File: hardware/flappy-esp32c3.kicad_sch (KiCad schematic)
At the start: 57 parts, among them J1 USB-C-Breakout 16P, J2 LiPo 1S 500 mAh, J3 OLED SSD1306 SPI, J4 Arcade-Taster, SW1 Ein/Aus, U1 ESP32-C3-WROOM-02-N4, U2 MCP73831-2-OT, U3 AP2112K-3.3

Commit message: Layout an den Schaltplan angleichen und auf 72 x 51 mm verkleinern
Abgleich Schaltplan <-> Layout
-----------------------------
Der Schaltplan war von Hand nachbearbeitet worden: R17/R18 (5k1) als
CC-Widerstaende an J1-5/J1-6. Weder gen/design.py noch die Platinendatei
kannten sie - die Platine haette keine CC-Widerstaende gehabt und mit einer
C-nach-C-Leitung kein VBUS bekommen.

R17/R18 stehen jetzt mit den Netzen CC1/CC2 in gen/design.py, J1-5 und J1-6
sind aus NO_CONNECT heraus. Sonst waren beide Dateien deckungsgleich.
Nach der Neuerzeugung: 0 Abweichungen (unabhaengig nachgerechnet).

Flaeche und Handbestueckbarkeit
-------------------------------
90 x 60 mm (5400 mm2) -> 72 x 51 mm (3672 mm2), 32 Prozent weniger.

Die alte Platine war zu 27 Prozent gefuellt und hatte trotzdem Stellen mit
0,15 mm Umrissabstand (LS1/R13, C9/R5, C9/U1, C8/R6) - der Platz lag als
leeres Band herum statt zwischen den Bauteilen. Jetzt gilt als pruefbare
Regel LOETABSTAND = 0,8 mm und RANDABSTAND = 0,5 mm; kleinster Wert im
Entwurf 0,82 mm. chk_place.py bricht ab, wenn es enger wird.

Leiterbahnen 843 -> 725 mm, Vias 113 -> 87, laengstes Rueckseitenstueck
10,8 -> 5,4 mm. C8 am Modulpin 10,8 -> 5,0 mm.

Weitere Befunde
---------------
* Die VBAT-Kuehlflaeche des Ladereglers lag nicht am Gehaeuse von U2,
  sondern nur ueber eine 0,5-mm-Bahn angebunden daneben - thermisch
  wirkungslos. Sie liegt jetzt unmittelbar am VBAT-Pad (122 mm2).
  chk_place.py prueft neu, dass jede NETZONE ein Pad ihres Netzes enthaelt;
  sonst wirft KiCad sie beim Fuellen als Insel wieder weg.
* Der Verdrahter reservierte nur fuer die eingeklemmten Masse-Mittelpins
  vorab ein Via. D1-5 (VBUS am ESD-Array) ist genauso eingeklemmt und fehlte.
  Liste heisst jetzt VORAB_VIA und nimmt den Netznamen aus der Netzliste.
* Die bauteil- und bahnfreien Flaechen unter Funkmodul und USB-C-Breakout
  waren als feste Koordinaten im Verdrahter verdrahtet. Sie werden jetzt aus
  der Platzierung abgeleitet und wandern beim Ve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
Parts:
- R17, R18: value 5.1k -> 5k1
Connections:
- net CC1: now reaches J1.5 (Pin_5), R17.1
- net CC2: now reaches J1.6 (Pin_6), R18.1
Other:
- note added: "Nur bestuecken, wenn das Breakout selbst keine CC-Widerstaende traegt."
- note added: "R17/R18 = 5k1 (Rd): ohne sie liefert eine C-nach-C-Leitung kein VBUS."

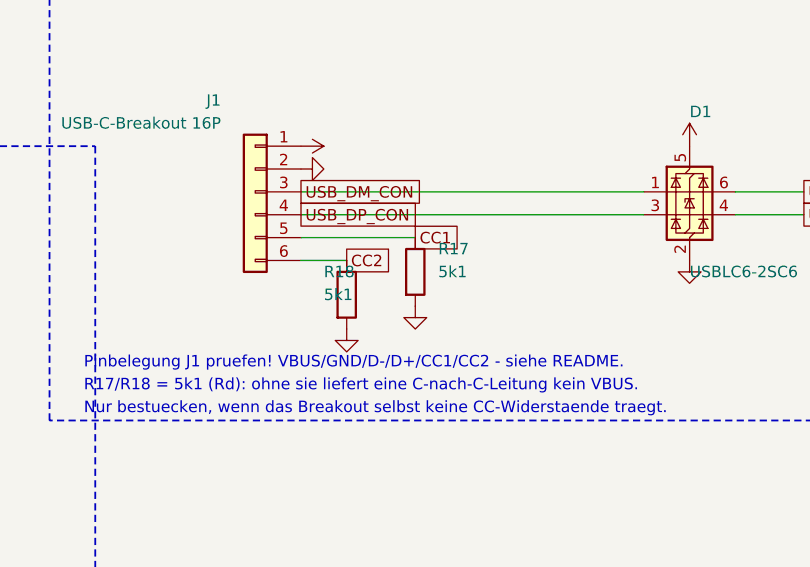
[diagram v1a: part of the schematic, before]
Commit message: Pruefbericht nachgerechnet: Wert nach .sch, Pfade portabel, Repo aufgeraeumt
Nachgeprueft wurden die Befunde F1-F5 eines externen Berichts. F1, F2 und F3
sind berechtigt, F4 und F5 sind bereits dokumentierte Handlungspunkte, keine
Fehler. Die Messwerte des Berichts gehoeren zu Revision A (90 x 60 mm,
371 Bahnen) und stimmen bis auf zwei Abstaende, die von der Masseseite der
Kondensatoren gemessen wurden.

.sch als Master
---------------
Vollstaendiger Abgleich des erzeugten Schaltplans gegen die von Hand
gezeichnete Fassung auf main: 57 Bauteile, 41 Netze, gleiche Footprints,
gleiche Nichtanschluesse - genau eine Abweichung. R17/R18 hiessen von Hand
5.1k, in design.py 5k1. Der Schaltplan gewinnt: design.py sagt jetzt 5.1k.

Der Wertepruefer in tests.py kannte die Schreibweise mit Dezimalpunkt nicht
und haette 5.1k als unlesbar gemeldet. Er nimmt jetzt beide Formen (6k8 und
5.1k); _wert() rechnete schon vorher beide richtig um.

F2: feste macOS-Pfade
---------------------
erzeugen.sh, gen/design.py und gen/tests_stufe3.py hatten
/Applications/KiCad/... fest verdrahtet und brachen auf Linux und Windows ab.
Alle drei suchen jetzt selbst: eigene Umgebungsvariable, dann PATH bzw.
KICAD*_SYMBOL_DIR/KICAD*_FOOTPRINT_DIR, dann die ueblichen Installationsorte
von macOS, Linux und Windows. Notausgang sind FLAPPY_KICAD_CLI,
FLAPPY_KICAD_SYMBOLS und FLAPPY_KICAD_FOOTPRINTS. Findet erzeugen.sh kein
kicad-cli, bricht es gleich am Anfang ab statt auf halbem Weg.

F3: Git-Hygiene
---------------
.DS_Store (zwei Stueck) und _restore_backup_2026-08-25T08-33-44-858/ waren
getrackt, obwohl .DS_Store schon in .gitignore stand. Beide aus der
Versionsverwaltung genommen, _restore_backup_*/ ergaenzt. Das Backup enthielt
den Stand vor der Handaenderung (54 Bauteile, ohne R17/R18) und ist damit
inhaltlich ueberholt.

Nebenbei gefunden
-----------------
pruefbericht.md nannte fuer Revision A 8,1 % Rueckseitenanteil (69 mm von
860 mm). Nachgemessen an der eingecheckten Fassung sind es 8,4 % (7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
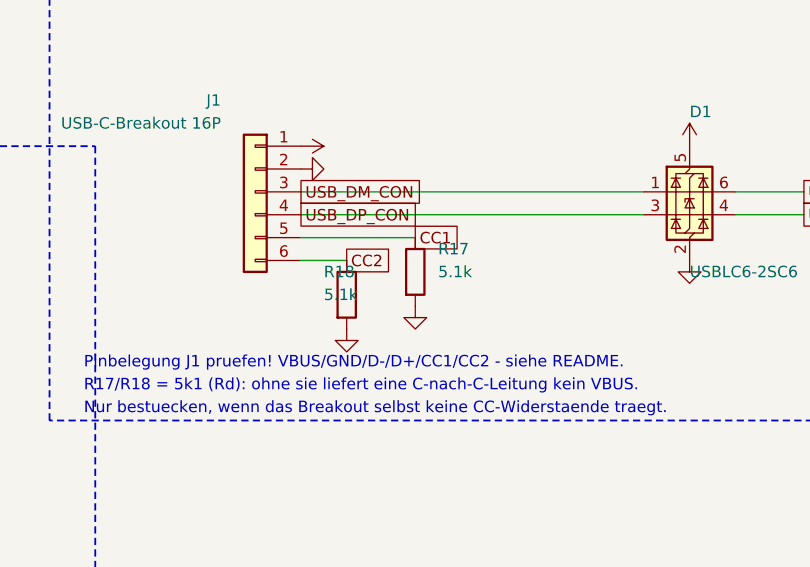
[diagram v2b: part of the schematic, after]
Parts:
- R17, R18: value 5k1 -> 5.1k
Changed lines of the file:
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@@
 			)
 		)
-		(property "Value" "5k1"
+		(property "Value" "5.1k"
 			(at 340.36 54.61 0)
 			(effects
@@
 			)
 		)
-		(property "Value" "5k1"
+		(property "Value" "5.1k"
 			(at 327.66 57.15 0)
 			(effects
